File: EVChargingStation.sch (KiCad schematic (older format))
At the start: 65 parts, among them J1 Connector1, J2 Connector1, J3 FC68131, J4 FC68131, J5 FC68131, K1 G5NB-1A Relay 5VDC, Q1 PN2222A, T1 VB_05-1-12, T2 VB_05-1-12, T3 VB_05-1-12, U1 ABX00027, U2 IRM-05-5, U3 LF353P, U4 mcp6291-e_p-nd, U5 mcp6291-e_p-nd, U6 mcp6291-e_p-nd

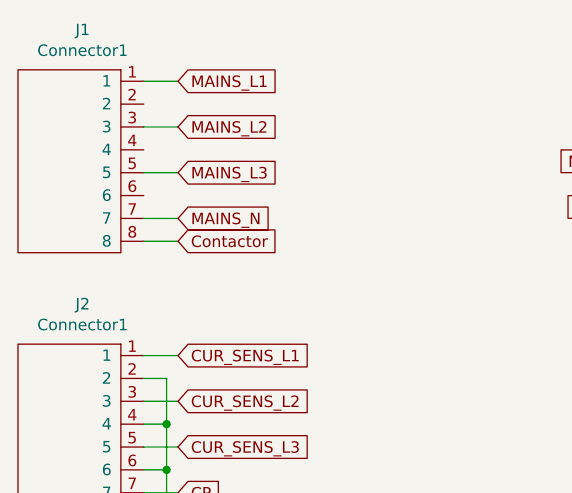
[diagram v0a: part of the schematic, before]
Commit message: revision 1.2 - added connection to PE
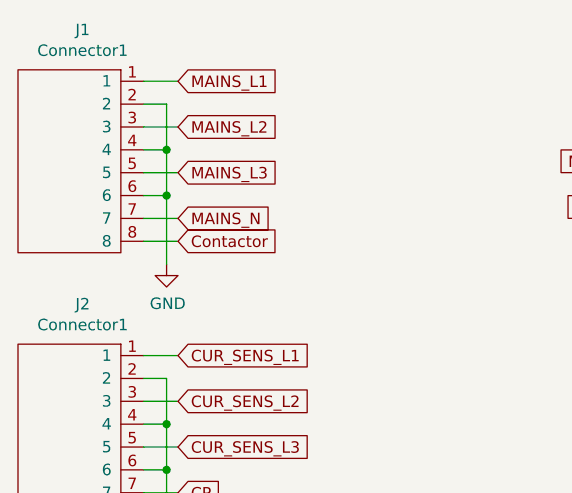
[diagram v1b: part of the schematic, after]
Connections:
- net GND: now also J1.2, J1.4, J1.6
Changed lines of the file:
@@
 Title "Dehne EV Charging Station"
 Date "2021-02-20"
-Rev "1"
+Rev "1.2"
 Comp "dehnes.com"
 Comment1 ""
@@
 Wire Wire Line
 	9750 3850 10650 3850
+$Comp
+L power:GND #PWR0130
+U 1 1 60347ADD
+P 1900 2100
+F 0 "#PWR0130" H 1900 1850 50  0001 C CNN
+F 1 "GND" H 1905 1927 50  0000 C CNN
+F 2 "" H 1900 2100 50  0001 C CNN
+F 3 "" H 1900 2100 50  0001 C CNN
+	1    1900 2100
+	1    0    0    -1
+$EndComp
+Wire Wire Line
+	1800 1400 1900 1400
+Wire Wire Line
+	1900 1400 1900 1600
+Wire Wire Line
+	1800 1600 1900 1600
+Connection ~ 1900 1600
+Wire Wire Line
+	1900 1600 1900 1800
+Wire Wire Line
+	1800 1800 1900 1800
+Connection ~ 1900 1800
+Wire Wire Line
+	1900 1800 1900 2100
 $EndSCHEMATC

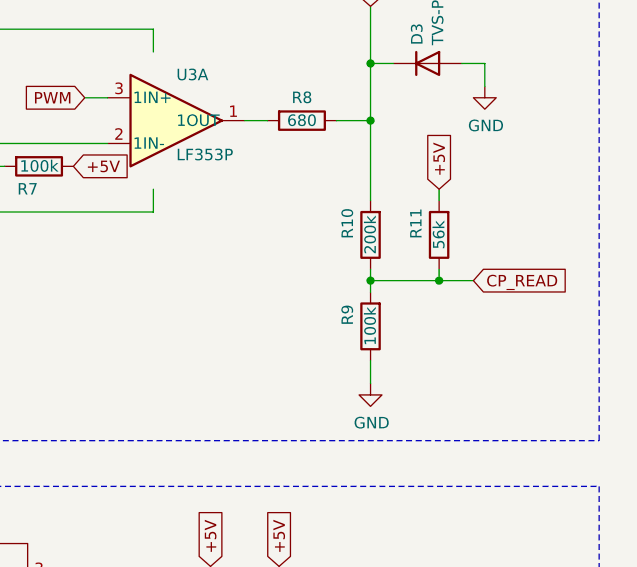
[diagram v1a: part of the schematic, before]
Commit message: Updated some resistor values & Readme
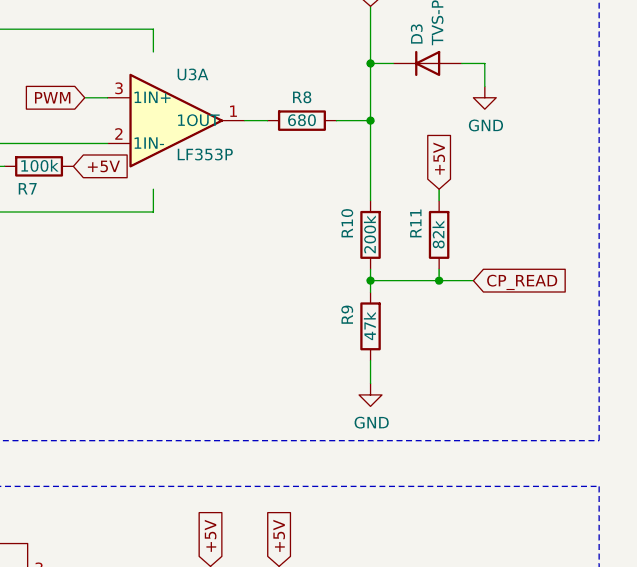
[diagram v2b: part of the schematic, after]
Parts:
- R11: value 56k -> 82k
- R9: value 100k -> 47k
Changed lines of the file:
@@
 P 11600 5150
 F 0 "R9" V 11700 5100 50  0000 C CNN
-F 1 "100k" V 11600 5150 50  0000 C CNN
+F 1 "47k" V 11600 5150 50  0000 C CNN
 F 2 "Resistor_THT:R_Axial_DIN0207_L6.3mm_D2.5mm_P10.16mm_Horizontal" V 11530 5150 50  0001 C CNN
 F 3 "~" H 11600 5150 50  0001 C CNN
@@
 P 11900 4750
 F 0 "R11" V 12000 4700 50  0000 C CNN
-F 1 "56k" V 11900 4750 50  0000 C CNN
+F 1 "82k" V 11900 4750 50  0000 C CNN
 F 2 "Resistor_THT:R_Axial_DIN0207_L6.3mm_D2.5mm_P10.16mm_Horizontal" V 11830 4750 50  0001 C CNN
 F 3 "~" H 11900 4750 50  0001 C CNN

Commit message: Working on revision 1.3
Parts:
- removed D1: 1N4148, Diode_THT:D_DO-35_SOD27_P7.62mm_Horizontal, symbol Device:D
- added unit 2 of U3
- added unit 3 of U3
- R2: value 10k -> 1k
- R6, R7: value 100k -> 120k
- R8: value 680 -> 1k
- U3: footprint Package_DIP:DIP-8_W7.62mm -> (none)
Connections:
- net +12VDC: now also U3.8 (Vcc+)
- net +5V: now also R1.2; no longer R1.1, R7.1
- net -12VDC: now also U3.4 (Vcc-)
- net GND: now also R2.1, R6.1, U3.5 (2IN+); no longer R6.2
- net PP: now also R1.1, U1.4 (A0/DAC0); no longer R1.2
- net +3V3: now reaches U1.2 (+3V3)
- net +3V3: now also R7.2
- removed net PP_READ: R2.1, U1.4 (A0/DAC0)
- new net: R6.2, R7.1, U3.2 (1IN-)
- new net: U3.6 (2IN-), U3.7 (2OUT)
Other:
- moved on the sheet: C1, C2, C3, D2, D3, K1, L1, PS1, Q1, R1, R10, R11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

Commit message: PCB layout for rev 1.3
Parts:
- removed D10, D12, D8: BZX85C4V7-TAP, Diode_THT:D_DO-41_SOD81_P7.62mm_Horizontal, symbol Device:D_Zener
- removed D11, D4, D5, D6, D7, D9: BZX85C3V0-TAP, Diode_THT:D_DO-41_SOD81_P7.62mm_Horizontal, symbol Device:D_Zener
- removed J2: Connector1, EVChargingStation:conn_08x02_wago, symbol EVChargingStationParts:Connector1
- removed R23: 10k, Resistor_THT:R_Axial_DIN0207_L6.3mm_D2.5mm_P10.16mm_Horizontal, symbol Device:R
- removed R24, R28, R31: 27k, Resistor_THT:R_Axial_DIN0207_L6.3mm_D2.5mm_P10.16mm_Horizontal, symbol Device:R
- removed R25, R27, R30: 4.7k, Resistor_THT:R_Axial_DIN0207_L6.3mm_D2.5mm_P10.16mm_Horizontal, symbol Device:R
- removed R29, R32: 8.2k, Resistor_THT:R_Axial_DIN0207_L6.3mm_D2.5mm_P10.16mm_Horizontal, symbol Device:R
- added D1, D4, D5: 1N4148, Diode_THT:D_DO-35_SOD27_P7.62mm_Horizontal, symbol Device:D
- R12, R16, R20: value 2.7k -> 10k
- R13: value 8.2k -> 10k
- R14, R18, R22: value 120k -> 10k
- R17, R21, R26: value 8.2k -> 100k
- U3: footprint (none) -> Package_DIP:DIP-8_W7.62mm
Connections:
- net +3V3: now also U4.4 (V+), U5.4 (V+), U6.4 (V+)
- net +5V: now also K1.4; no longer K1.1, R14.2, R18.2, R22.2, R26.2, U4.4 (V+), U5.4 (V+), U6.4 (V+)
- net CP: now also J1.7
- net CURRENT_SENS_L2_READ: now also R16.2; no longer R17.2
- net CURRENT_SENS_L3_READ: now also R20.2; no longer R21.2
- net CUR_SENS_L1: now also U4.3 (+); no longer R15.1
- net CUR_SENS_L2: now also U5.3 (+); no longer R19.1
- net CUR_SENS_L3: now also U6.3 (+)
- net Contactor: now also J1.5; no longer J1.8
- net GND: now also R14.2, R15.1, R18.2, R19.1, R22.2; no longer J1.2, J1.4, J1.6, R16.1, R20.1
- net MAINS_L1: now also J1.4, K1.2; no longer J1.1
- net MAINS_L3: now also J1.2; no longer J1.5, K1.2
- net MAINS_N: now also J1.1; no longer J1.7
- net PP: now also J1.8
- net VOLTAGE_SENS_L1_READ: now also R14.1, R26.2; no longer R26.1
- net VOLTAGE_SENS_L2_READ: now also R17.2, R18.1
- net VOLTAGE_SENS_L3_READ: now also R21.2, R22.1
- net at D2.2 (A), Q1.3 (C): now also K1.1; no longer K1.4
- net at T1.3 (SEC_1): now also D1.2 (A)
- net at T2.3 (SEC_1): now also D4.2 (A)
- net at T3.3 (SEC_1): now also D5.2 (A)
- new net: D1.1 (K), R26.1
- new net: D4.1 (K), R17.1
- new net: D5.1 (K), R21.1
- new net: R15.2, R16.1, U5.2 (-)
- new net: R19.2, R20.1, U6.2 (-)
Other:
- moved on the sheet: J1, J3, J4, J5, R1, R12, R13, R2, R26, U1, U2, U4

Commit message: revision 1.3 done
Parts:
- removed R11: 82k, Resistor_THT:R_Axial_DIN0207_L6.3mm_D2.5mm_P10.16mm_Horizontal, symbol Device:R
- removed R4, R5: 2k, Resistor_THT:R_Axial_DIN0207_L6.3mm_D2.5mm_P10.16mm_Horizontal, symbol Device:R
- added D6: 1N4148, Diode_THT:D_DO-35_SOD27_P7.62mm_Horizontal, symbol Device:D
- PS1: value IA0512S -> NMA0512SC
- R7: renamed from R10; value 200k -> 180k
- U1: value ABX00027 -> Arduino Nano 33 IoT
- U3: value LF353P -> LT1498IN8#PBF
- renumbered R26 to R10, R18 to R11, R17 to R12, R22 to R13, R21 to R14, R12 to R15, R13 to R16, R15 to R17, R16 to R18, R6 to R4, R7 to R5, R8 to R6, R9 to R8, R14 to R9
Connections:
- net CP: now also D6.2 (A); no longer R7.2
- new net: D6.1 (K), R7.2
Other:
- moved on the sheet: D3, R4, R5, R6, U3A, U3C
